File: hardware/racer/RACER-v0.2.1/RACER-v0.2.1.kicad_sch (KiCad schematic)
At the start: 0 parts

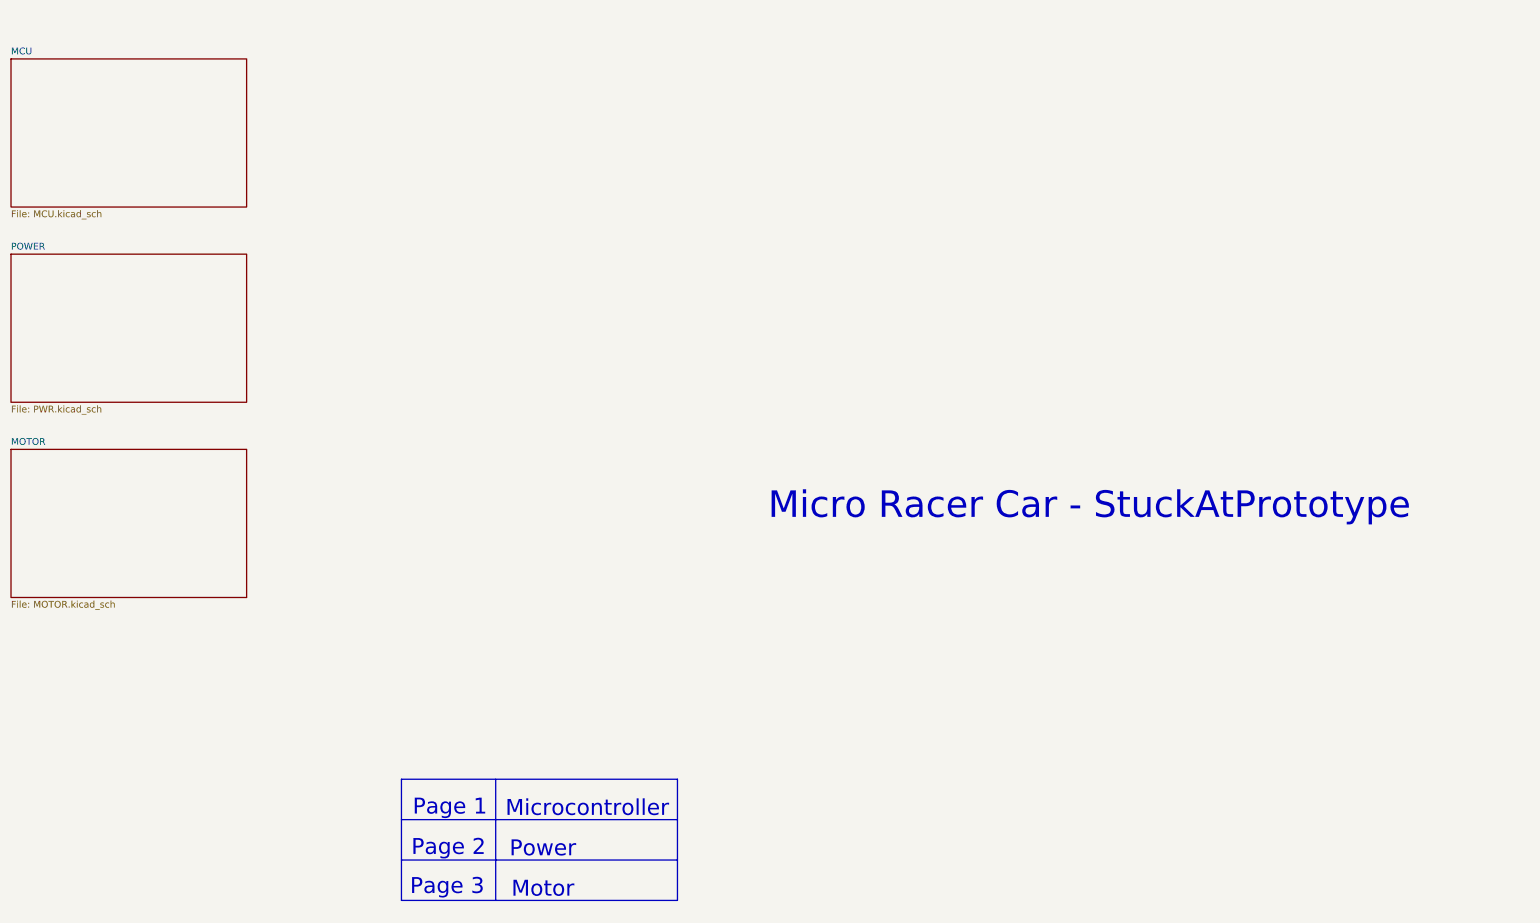
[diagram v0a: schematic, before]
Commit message: Schematic improvement & LCSC BOM
- Schematic readability improvements.
- Changed schematic symbols.
- Changed to hierarchical schematic.
- Added LCSC BOM for the available components.
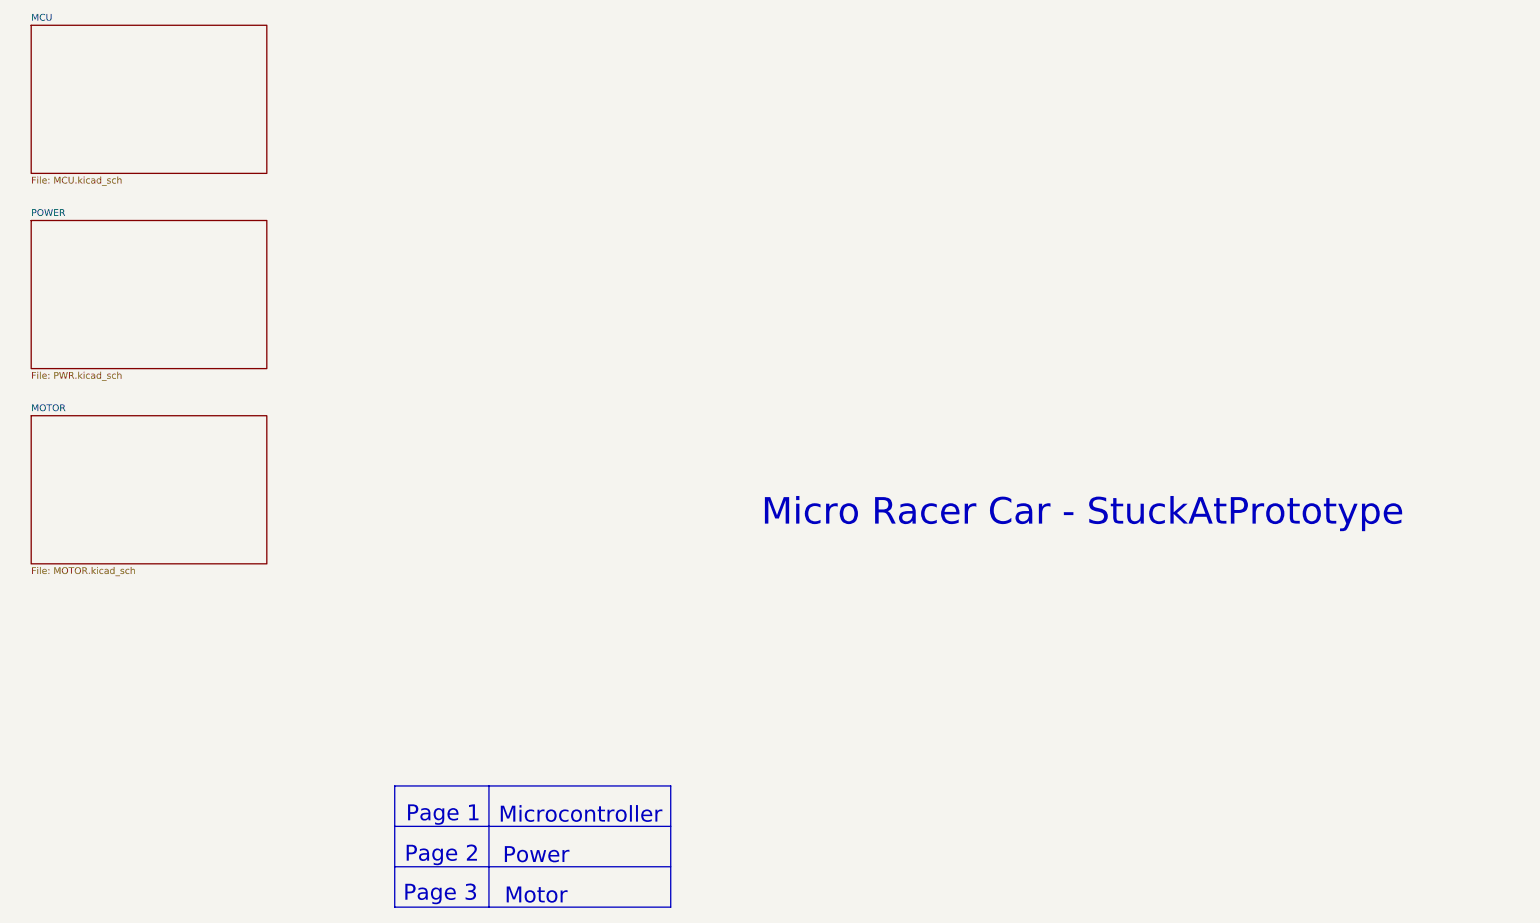
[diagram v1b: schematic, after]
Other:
- company: StuckAtPrototype -> (none)
- title: Racer -> Micro Racer Car
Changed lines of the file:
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@@
 	(paper "A4")
 	(title_block
-		(title "Racer")
-		(date "2024-10-14")
-		(rev "v0.2")
-		(company "StuckAtPrototype")
+		(title "Micro Racer Car")
+		(date "2024-10-17")
+		(rev "0.2.1")
 	)
 	(polyline
 		(pts
-			(xy 36.83 168.91) (xy 36.83 191.77)
+			(xy 35.56 170.18) (xy 35.56 193.04)
 		)
 		(stroke
@@
 	(polyline
 		(pts
-			(xy 19.05 184.15) (xy 71.12 184.15)
+			(xy 17.78 177.8) (xy 69.85 177.8)
 		)
 		(stroke
@@
 	(polyline
 		(pts
-			(xy 19.05 176.53) (xy 71.12 176.53)
+			(xy 17.78 185.42) (xy 69.85 185.42)
 		)
 		(stroke
@@
 	)
 	(rectangle
-		(start 19.05 168.91)
-		(end 71.12 191.77)
+		(start 17.78 170.18)
+		(end 69.85 193.04)
 		(stroke
 			(width 0.2)
@@
 	)
 	(image
-		(at 147.8499 73.1165)
+		(at 146.5799 74.3865)
 		(scale 0.405702)
 		(data "iVBORw0KGgoAAAANSUhEUgAAAtAAAAHgCAIAAAADp837AAAABGdBTUEAALGPC/xhBQAACklpQ0NQ"
@@
 		)
 	)
-	(text "Micro Racer Car - StuckAtPrototype"
+	(text "Page 3"
 		(exclude_from_sim no)
-		(at 148.844 117.348 0)
+		(at 26.416 190.5 0)
 		(effects
 			(font
 				(face "Avenir")
-				(size 5 5)
-				(color 0 0 0 1)
+				(size 3 3)
 			)
 		)
 	)
-	(text "Page 1"
+	(text "Micro Racer Car - StuckAtPrototype"
 		(exclude_from_sim no)
-		(at 28.194 174.244 0)
+		(at 147.574 118.618 0)
 		(effects
 			(font
 				(face "Avenir")
-				(size 3 3)
+				(size 5 5)
+				(color 0 0 0 1)
 			)
 		)
 	)
-	(text "Power"
+	(text "Microcontroller"
 		(exclude_from_sim no)
-		(at 45.72 182.118 0)
+		(at 52.832 175.768 0)
 		(effects
 			(font
@@
 		)
 	)
-	(text "Page 3"
+	(text "Power"
 		(exclude_from_sim no)
-		(at 27.686 189.23 0)
+		(at 44.45 183.388 0)
 		(effects
 			(font
@@
 		)
 	)
-	(text "Microcontroller"
+	(text "Motor"
 		(exclude_from_sim no)
-		(at 54.102 174.498 0)
+		(at 44.45 191.008 0)
 		(effects
 			(font
@@
 	(text "Page 2\n"
 		(exclude_from_sim no)
-		(at 27.94 181.864 0)
+		(at 26.67 183.134 0)
 		(effects
 			(font
@@
 		)
 	)
-	(text "Motor"
+	(text "Page 1"
 		(exclude_from_sim no)
-		(at 45.72 189.738 0)
+		(at 26.924 175.514 0)
 		(effects
 			(font
@@
 	)
 	(sheet
-		(at -54.61 106.68)
+		(at -50.8 63.5)
 		(size 44.45 27.94)
 		(fields_autoplaced yes)
@@
 			(color 0 0 0 0.0000)
 		)
-		(property "Sheetname" "MOTOR"
-			(at -54.61 105.9684 0)
+		(property "Sheetname" "POWER"
+			(at -50.8 62.7884 0)
 			(effects
 				(font
@@
 			)
 		)
-		(property "Sheetfile" "MOTOR.kicad_sch"
-			(at -54.61 135.2046 0)
+		(property "Sheetfile" "PWR.kicad_sch"
+			(at -50.8 92.0246 0)
 			(effects
 				(font
@@
 		)
 		(instances
-			(project "racer"
-				(path "/11c7bd96-786c-4c10-b71b-7b198cc052d5"
+			(project "RACER-v0.2.1"
+				(path "/36bdd4b7-48c8-44dd-9605-574cba1acfde"
 					(page "3")
 				)
@@
 	)
 	(sheet
-		(at -54.61 69.85)
+		(at -50.8 100.33)
 		(size 44.45 27.94)
 		(fields_autoplaced yes)
@@
 			(color 0 0 0 0.0000)
 		)
-		(property "Sheetname" "POWER"
-			(at -54.61 69.1384 0)
+		(property "Sheetname" "MOTOR"
+			(at -50.8 99.6184 0)
 			(effects
 				(font
@@
 			)
 		)
-		(property "Sheetfile" "PWR.kicad_sch"
-			(at -54.61 98.3746 0)
+		(property "Sheetfile" "MOTOR.kicad_sch"
+			(at -50.8 128.8546 0)
 			(effects
 				(font
@@
 		)
 		(instances
-			(project "racer"
-				(path "/11c7bd96-786c-4c10-b71b-7b198cc052d5"
+			(project "RACER-v0.2.1"
+				(path "/36bdd4b7-48c8-44dd-9605-574cba1acfde"
 					(page "4")
 				)
@@
 	)
 	(sheet
-		(at -54.61 33.02)
+		(at -50.8 26.67)
 		(size 44.45 27.94)
 		(fields_autoplaced yes)
@@
 		)
 		(property "Sheetname" "MCU"
-			(at -54.61 32.3084 0)
+			(at -50.8 25.9584 0)
 			(effects
 				(font
@@
 		)
 		(property "Sheetfile" "MCU.kicad_sch"
-			(at -54.61 61.5446 0)
+			(at -50.8 55.1946 0)
 			(effects
 				(font
@@
 		)
 		(instances
-			(project "racer"
-				(path "/11c7bd96-786c-4c10-b71b-7b198cc052d5"
+			(project "RACER-v0.2.1"
+				(path "/36bdd4b7-48c8-44dd-9605-574cba1acfde"
 					(page "2")
 				)
